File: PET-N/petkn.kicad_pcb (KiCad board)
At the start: 2 copper layers, 386.1 x 99.6 mm, 83 parts, among them J1 Conn_01x20, J2 Conn_02x03_Odd_Even, J3 LINK3, J4 Conn_01x20, J5 SPACE1, J6 SPACE2, J67 LINK67, SW1 KP "=", SW10 KP "0", SW11 R SHIFT, SW12 ">", SW14 "]", SW15 "@", SW16 L SHIFT, SW17 KP "+", SW18 KP "2", SW2 KP ".", SW20 "?", SW21 ",", SW22 "N", SW23 "V", SW24 "X", SW25 KP "3", SW26 KP "1", SW27 RETURN, SW28 ";", SW29 "M", SW3 NC ($10), SW30 "B", SW31 "C", SW32 "Z", SW320 S LOCK, SW33 KP "*", SW34 KP "5", SW36 ":", SW37 "K", SW38 "H", SW39 "F", SW4 STOP, SW40 "S", SW41 KP "6", SW42 KP "4", SW44 "L", SW45 "J", SW46 "G", SW47 "D", SW48 "A", SW49 KP "/", SW5 "<", SW50 KP "8", SW52 "P", SW53 "I", SW54 "Y", SW55 "R", SW56 "W", SW57 KP "9", SW58 KP "7", SW59 U ARROW, SW6 SPACE, SW60 "O", SW61 "U", SW62 "T", SW63 "E", SW64 "Q", SW65 INS/DEL, SW66 UP/DOWN, SW67 NC ($0A), SW68 ")", SW69 "\", SW7 "[", SW70 "'", SW71 "$", SW72 QUOTE, SW73 LEFT/RIGHT, SW74 CLR/HOME, SW75 B ARROW, SW76 "(", SW77 "&", SW78 "%", SW79 "#"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

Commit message: first work on adding LEDs and extended connector
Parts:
- removed J4: Conn_01x20, Connector_PinHeader_2.54mm:PinHeader_1x20_P2.54mm_Vertical
- J1: value Conn_01x20 -> Extended_PET_keyboard_connector; footprint Connector_PinHeader_2.54mm:PinHeader_1x20_P2.54mm_Vertical -> petkn:PET_Extended_Keyboard_Connector
- SW1, SW10, SW12, SW14, SW15, SW17, SW18, SW2, SW20, SW21, SW22, SW23, SW24, SW25, SW26, SW28, SW29, SW30, SW31, SW32, SW33, SW34, SW36, SW37, SW38, SW39, SW4, SW40, SW41, SW42, SW44, SW45, SW46, SW47, SW48, SW49, SW5, SW50, SW52, SW53, SW54, SW55, SW56, SW57, SW58, SW59, SW60, SW61, SW62, SW63, SW64, SW65, SW66, SW68, SW69, SW7, SW70, SW71, SW72, SW73, SW74, SW75, SW76, SW77, SW78, SW79, SW80, SW9: footprint Button_Switch_Keyboard:SW_Cherry_MX_1.00u_PCB -> petkn:SW_Cherry_MX_1.00u_PCB_with_LED
- SW11, SW16: footprint Button_Switch_Keyboard:SW_Cherry_MX_2.00u_PCB -> petkn:SW_Cherry_MX_2.00u_PCB_with_LED
- SW27, SW320, SW8: footprint Button_Switch_Keyboard:SW_Cherry_MX1A_1.50u_PCB -> petkn:SW_Cherry_MX_1.50u_PCB_with_LED
- SW3: footprint Button_Switch_Keyboard:SW_Cherry_MX1A_1.25u_PCB -> petkn:SW_Cherry_MX_1.25u_PCB_with_LED
- SW6: footprint Button_Switch_Keyboard:SW_Cherry_MX1A_6.25u_PCB -> petkn:SW_Cherry_MX_6.25u_PCB_with_LED
- SW67: footprint Button_Switch_Keyboard:SW_Cherry_MX_1.50u_PCB -> petkn:SW_Cherry_MX_1.50u_PCB_with_LED
- moved J1 1.93 mm to (234.1, 48.6)
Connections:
- J1 pad 1: (no net) -> GND
- J1 pad 2: (no net) -> unconnected-(J1-key-Pad2)
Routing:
- net C1: track 509.6 -> 371.9 mm
- net C2: track 509.5 -> 460.9 mm
- net R10: track 641.0 -> 598.0 mm, vias 1 -> 0
- net C4: track 304.8 -> 262.5 mm
- net C3: track 437.6 -> 405.7 mm
- net C6: track 504.1 -> 474.5 mm
- net R9: track 590.0 -> 563.2 mm
- net C5: track 252.0 -> 233.5 mm, vias 2 -> 1
- net C8: track 377.6 -> 371.5 mm
- net R2: track 601.0 -> 595.3 mm, vias 5 -> 6
- net R1: track 440.7 -> 437.4 mm, vias 4 -> 5
- net C7: track 345.6 -> 343.2 mm
- net R6: vias 4 -> 5
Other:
- board size 386.1 x 99.6 mm -> 386.1 x 102 mm
- board text added: "{dblquote}N-V2.1{dblquote} (C) A. Fachat, 2025-05-31"
- board text removed: "20 19 18 17 16 15 14 13 12 11 10 9 8 7 6 5 4 3 2 1"
- board text removed: "C1 C2 C3 C4 C5 C6 C7 C8 R1 R2 R3 R4 R5 R6 R7 R8 R9 R10 NC GND"

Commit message: add extension page, add 4-to-10 decoder
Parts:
- added C1: C, Capacitor_THT:C_Disc_D4.3mm_W1.9mm_P5.00mm, F.Cu at (303.7, 60.1)
- added U1: 74LS145, Package_DIP:DIP-16_W7.62mm, F.Cu at (302.5, 64.3)
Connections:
- SW1 pad 3: (no net) -> unconnected-(SW1B-K-Pad3)
- SW1 pad 4: (no net) -> unconnected-(SW1B-A-Pad4)
- SW10 pad 3: (no net) -> unconnected-(SW10B-K-Pad3)
- SW10 pad 4: (no net) -> unconnected-(SW10B-A-Pad4)
- SW11 pad 3: (no net) -> unconnected-(SW11B-K-Pad3)
- SW11 pad 4: (no net) -> unconnected-(SW11B-A-Pad4)
- SW12 pad 3: (no net) -> unconnected-(SW12B-K-Pad3)
- SW12 pad 4: (no net) -> unconnected-(SW12B-A-Pad4)
- SW14 pad 3: (no net) -> unconnected-(SW14B-K-Pad3)
- SW14 pad 4: (no net) -> unconnected-(SW14B-A-Pad4)
- SW15 pad 3: (no net) -> unconnected-(SW15B-K-Pad3)
- SW15 pad 4: (no net) -> unconnected-(SW15B-A-Pad4)
- SW16 pad 3: (no net) -> unconnected-(SW16B-K-Pad3)
- SW16 pad 4: (no net) -> unconnected-(SW16B-A-Pad4)
- SW17 pad 3: (no net) -> unconnected-(SW17B-K-Pad3)
- SW17 pad 4: (no net) -> unconnected-(SW17B-A-Pad4)
- SW18 pad 3: (no net) -> unconnected-(SW18B-K-Pad3)
- SW18 pad 4: (no net) -> unconnected-(SW18B-A-Pad4)
- SW2 pad 3: (no net) -> unconnected-(SW2B-K-Pad3)
- SW2 pad 4: (no net) -> unconnected-(SW2B-A-Pad4)
- SW20 pad 3: (no net) -> unconnected-(SW20B-K-Pad3)
- SW20 pad 4: (no net) -> unconnected-(SW20B-A-Pad4)
- SW21 pad 3: (no net) -> unconnected-(SW21B-K-Pad3)
- SW21 pad 4: (no net) -> unconnected-(SW21B-A-Pad4)
- SW22 pad 3: (no net) -> unconnected-(SW22B-K-Pad3)
- SW22 pad 4: (no net) -> unconnected-(SW22B-A-Pad4)
- SW23 pad 3: (no net) -> unconnected-(SW23B-K-Pad3)
- SW23 pad 4: (no net) -> unconnected-(SW23B-A-Pad4)
- SW24 pad 3: (no net) -> unconnected-(SW24B-K-Pad3)
- SW24 pad 4: (no net) -> unconnected-(SW24B-A-Pad4)
- SW25 pad 3: (no net) -> unconnected-(SW25B-K-Pad3)
- SW25 pad 4: (no net) -> unconnected-(SW25B-A-Pad4)
- SW26 pad 3: (no net) -> unconnected-(SW26B-K-Pad3)
- SW26 pad 4: (no net) -> unconnected-(SW26B-A-Pad4)
- SW27 pad 3: (no net) -> unconnected-(SW27B-K-Pad3)
- SW27 pad 4: (no net) -> unconnected-(SW27B-A-Pad4)
- SW28 pad 3: (no net) -> unconnected-(SW28B-K-Pad3)
- SW28 pad 4: (no net) -> unconnected-(SW28B-A-Pad4)
- SW29 pad 3: (no net) -> unconnected-(SW29B-K-Pad3)
- SW29 pad 4: (no net) -> unconnected-(SW29B-A-Pad4)
- SW3 pad 3: (no net) -> unconnected-(SW3B-K-Pad3)
- SW3 pad 4: (no net) -> unconnected-(SW3B-A-Pad4)
- SW30 pad 3: (no net) -> unconnected-(SW30B-K-Pad3)
- SW30 pad 4: (no net) -> unconnected-(SW30B-A-Pad4)
- SW31 pad 3: (no net) -> unconnected-(SW31B-K-Pad3)
- SW31 pad 4: (no net) -> unconnected-(SW31B-A-Pad4)
- SW32 pad 3: (no net) -> unconnected-(SW32B-K-Pad3)
- SW32 pad 4: (no net) -> unconnected-(SW32B-A-Pad4)
- SW320 pad 3: (no net) -> unconnected-(SW320B-K-Pad3)
- SW320 pad 4: (no net) -> unconnected-(SW320B-A-Pad4)
- SW33 pad 3: (no net) -> unconnected-(SW33B-K-Pad3)
- SW33 pad 4: (no net) -> unconnected-(SW33B-A-Pad4)
- SW34 pad 3: (no net) -> unconnected-(SW34B-K-Pad3)
- SW34 pad 4: (no net) -> unconnected-(SW34B-A-Pad4)
- SW36 pad 3: (no net) -> unconnected-(SW36B-K-Pad3)
- SW36 pad 4: (no net) -> unconnected-(SW36B-A-Pad4)
- SW37 pad 3: (no net) -> unconnected-(SW37B-K-Pad3)
- SW37 pad 4: (no net) -> unconnected-(SW37B-A-Pad4)
- SW38 pad 3: (no net) -> unconnected-(SW38B-K-Pad3)
- SW38 pad 4: (no net) -> unconnected-(SW38B-A-Pad4)
- SW39 pad 3: (no net) -> unconnected-(SW39B-K-Pad3)
- SW39 pad 4: (no net) -> unconnected-(SW39B-A-Pad4)
- SW4 pad 3: (no net) -> unconnected-(SW4B-K-Pad3)
- SW4 pad 4: (no net) -> unconnected-(SW4B-A-Pad4)
- SW40 pad 3: (no net) -> unconnected-(SW40B-K-Pad3)
- SW40 pad 4: (no net) -> unconnected-(SW40B-A-Pad4)
- SW41 pad 3: (no net) -> unconnected-(SW41B-K-Pad3)
- SW41 pad 4: (no net) -> unconnected-(SW41B-A-Pad4)
- SW42 pad 3: (no net) -> unconnected-(SW42B-K-Pad3)
- SW42 pad 4: (no net) -> unconnected-(SW42B-A-Pad4)
- SW44 pad 3: (no net) -> unconnected-(SW44B-K-Pad3)
- SW44 pad 4: (no net) -> unconnected-(SW44B-A-Pad4)
- SW45 pad 3: (no net) -> unconnected-(SW45B-K-Pad3)
- SW45 pad 4: (no net) -> unconnected-(SW45B-A-Pad4)
- SW46 pad 3: (no net) -> unconnected-(SW46B-K-Pad3)
- SW46 pad 4: (no net) -> unconnected-(SW46B-A-Pad4)
- SW47 pad 3: (no net) -> unconnected-(SW47B-K-Pad3)
- SW47 pad 4: (no net) -> unconnected-(SW47B-A-Pad4)
- SW48 pad 3: (no net) -> unconnected-(SW48B-K-Pad3)
- SW48 pad 4: (no net) -> unconnected-(SW48B-A-Pad4)
- SW49 pad 3: (no net) -> unconnected-(SW49B-K-Pad3)
- SW49 pad 4: (no net) -> unconnected-(SW49B-A-Pad4)
- SW5 pad 3: (no net) -> unconnected-(SW5B-K-Pad3)
- SW5 pad 4: (no net) -> unconnected-(SW5B-A-Pad4)
- SW50 pad 3: (no net) -> unconnected-(SW50B-K-Pad3)
- SW50 pad 4: (no net) -> unconnected-(SW50B-A-Pad4)
- SW52 pad 3: (no net) -> unconnected-(SW52B-K-Pad3)
- SW52 pad 4: (no net) -> unconnected-(SW52B-A-Pad4)
- SW53 pad 3: (no net) -> unconnected-(SW53B-K-Pad3)
- SW53 pad 4: (no net) -> unconnected-(SW53B-A-Pad4)
- SW54 pad 3: (no net) -> unconnected-(SW54B-K-Pad3)
- SW54 pad 4: (no net) -> unconnected-(SW54B-A-Pad4)
- SW55 pad 3: (no net) -> unconnected-(SW55B-K-Pad3)
- SW55 pad 4: (no net) -> unconnected-(SW55B-A-Pad4)
- SW56 pad 3: (no net) -> unconnected-(SW56B-K-Pad3)
- SW56 pad 4: (no net) -> unconnected-(SW56B-A-Pad4)
- SW57 pad 3: (no net) -> unconnected-(SW57B-K-Pad3)
- SW57 pad 4: (no net) -> unconnected-(SW57B-A-Pad4)
- SW58 pad 3: (no net) -> unconnected-(SW58B-K-Pad3)
- SW58 pad 4: (no net) -> unconnected-(SW58B-A-Pad4)
- SW59 pad 3: (no net) -> unconnected-(SW59B-K-Pad3)
- SW59 pad 4: (no net) -> unconnected-(SW59B-A-Pad4)
- SW6 pad 3: (no net) -> unconnected-(SW6B-K-Pad3)
- SW6 pad 4: (no net) -> unconnected-(SW6B-A-Pad4)
- SW60 pad 3: (no net) -> unconnected-(SW60B-K-Pad3)
- SW60 pad 4: (no net) -> unconnected-(SW60B-A-Pad4)
- SW61 pad 3: (no net) -> unconnected-(SW61B-K-Pad3)
- SW61 pad 4: (no net) -> unconnected-(SW61B-A-Pad4)
- SW62 pad 3: (no net) -> unconnected-(SW62B-K-Pad3)
- SW62 pad 4: (no net) -> unconnected-(SW62B-A-Pad4)
- SW63 pad 3: (no net) -> unconnected-(SW63B-K-Pad3)
- SW63 pad 4: (no net) -> unconnected-(SW63B-A-Pad4)
- SW64 pad 3: (no net) -> unconnected-(SW64B-K-Pad3)
- SW64 pad 4: (no net) -> unconnected-(SW64B-A-Pad4)
- SW65 pad 3: (no net) -> unconnected-(SW65B-K-Pad3)
- SW65 pad 4: (no net) -> unconnected-(SW65B-A-Pad4)
- SW66 pad 3: (no net) -> unconnected-(SW66B-K-Pad3)
- SW66 pad 4: (no net) -> unconnected-(SW66B-A-Pad4)
- SW67 pad 3: (no net) -> unconnected-(SW67B-K-Pad3)
- SW67 pad 4: (no net) -> unconnected-(SW67B-A-Pad4)
- SW68 pad 3: (no net) -> unconnected-(SW68B-K-Pad3)
- SW68 pad 4: (no net) -> unconnected-(SW68B-A-Pad4)
- SW69 pad 3: (no net) -> unconnected-(SW69B-K-Pad3)
- SW69 pad 4: (no net) -> unconnected-(SW69B-A-Pad4)
- SW7 pad 3: (no net) -> unconnected-(SW7B-K-Pad3)
- SW7 pad 4: (no net) -> unconnected-(SW7B-A-Pad4)
- SW70 pad 3: (no net) -> unconnected-(SW70B-K-Pad3)
- SW70 pad 4: (no net) -> unconnected-(SW70B-A-Pad4)
- SW71 pad 3: (no net) -> unconnected-(SW71B-K-Pad3)
- SW71 pad 4: (no net) -> unconnected-(SW71B-A-Pad4)
- SW72 pad 3: (no net) -> unconnected-(SW72B-K-Pad3)
- SW72 pad 4: (no net) -> unconnected-(SW72B-A-Pad4)
- SW73 pad 3: (no net) -> unconnected-(SW73B-K-Pad3)
- SW73 pad 4: (no net) -> unconnected-(SW73B-A-Pad4)
- SW74 pad 3: (no net) -> unconnected-(SW74B-K-Pad3)
- SW74 pad 4: (no net) -> unconnected-(SW74B-A-Pad4)
- SW75 pad 3: (no net) -> unconnected-(SW75B-K-Pad3)
- SW75 pad 4: (no net) -> unconnected-(SW75B-A-Pad4)
- SW76 pad 3: (no net) -> unconnected-(SW76B-K-Pad3)
- SW76 pad 4: (no net) -> unconnected-(SW76B-A-Pad4)
- SW77 pad 3: (no net) -> unconnected-(SW77B-K-Pad3)
- SW77 pad 4: (no net) -> unconnected-(SW77B-A-Pad4)
- SW78 pad 3: (no net) -> unconnected-(SW78B-K-Pad3)
- SW78 pad 4: (no net) -> unconnected-(SW78B-A-Pad4)
- SW79 pad 3: (no net) -> unconnected-(SW79B-K-Pad3)
- SW79 pad 4: (no net) -> unconnected-(SW79B-A-Pad4)
- SW8 pad 3: (no net) -> unconnected-(SW8B-K-Pad3)
- SW8 pad 4: (no net) -> unconnected-(SW8B-A-Pad4)
- SW80 pad 3: (no net) -> unconnected-(SW80B-K-Pad3)
- SW80 pad 4: (no net) -> unconnected-(SW80B-A-Pad4)
- SW9 pad 3: (no net) -> unconnected-(SW9B-K-Pad3)
- SW9 pad 4: (no net) -> unconnected-(SW9B-A-Pad4)
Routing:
- net R10: track 598.0 -> 0.00 mm
- net R2: track 595.3 -> 0.00 mm, vias 6 -> 0
- net R9: track 563.2 -> 0.00 mm, vias 5 -> 0
- net R4: track 532.2 -> 0.00 mm, vias 3 -> 0
- net C6: track 474.5 -> 0.00 mm, vias 6 -> 0
- net C2: track 460.9 -> 0.00 mm, vias 4 -> 0
- net R1: track 437.4 -> 0.00 mm, vias 5 -> 0
- net R8: track 430.2 -> 0.00 mm, vias 3 -> 0
- net R6: track 414.2 -> 0.00 mm, vias 5 -> 0
- net R7: track 410.3 -> 0.00 mm, vias 3 -> 0
- net C3: track 405.7 -> 0.00 mm, vias 2 -> 0
- net R3: track 384.7 -> 0.00 mm, vias 3 -> 0
- net R5: track 374.0 -> 0.00 mm, vias 1 -> 0
- net C1: track 371.9 -> 0.00 mm, vias 3 -> 0
- net C8: track 371.5 -> 0.00 mm, vias 1 -> 0
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
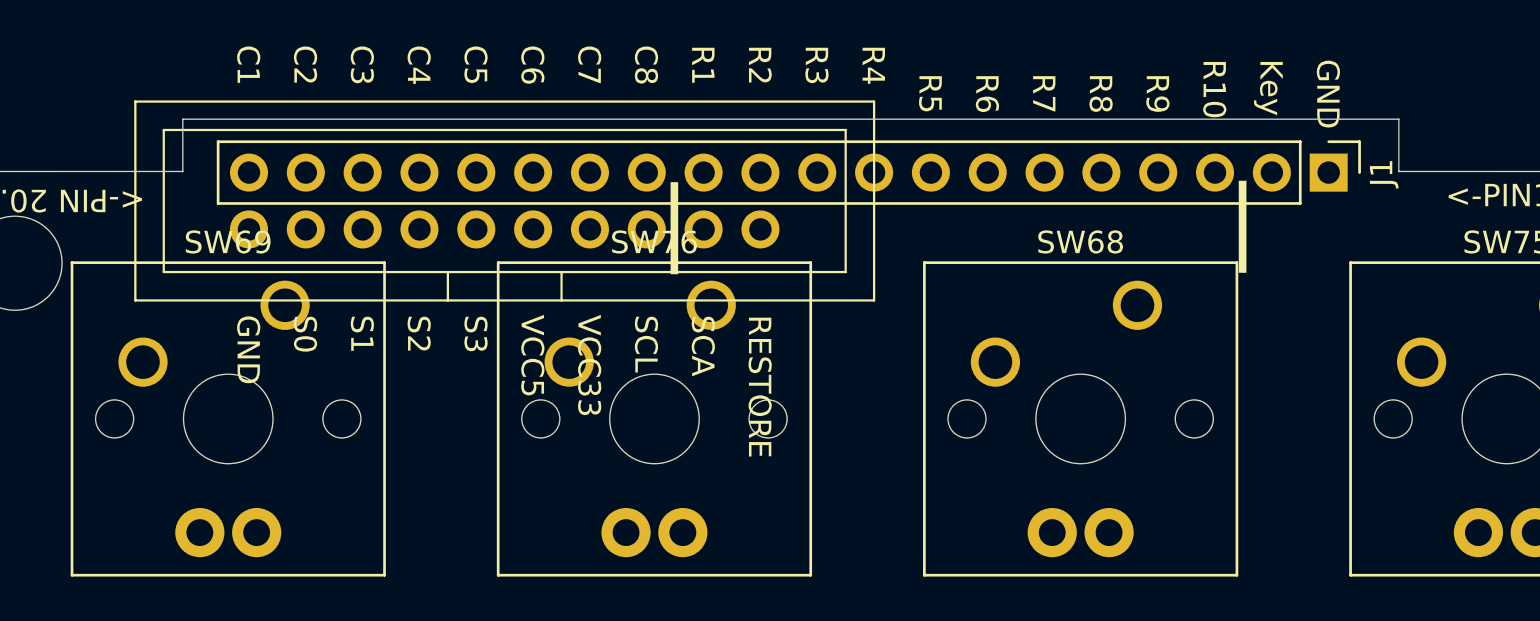
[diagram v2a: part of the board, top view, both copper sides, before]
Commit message: test board for LED drivers
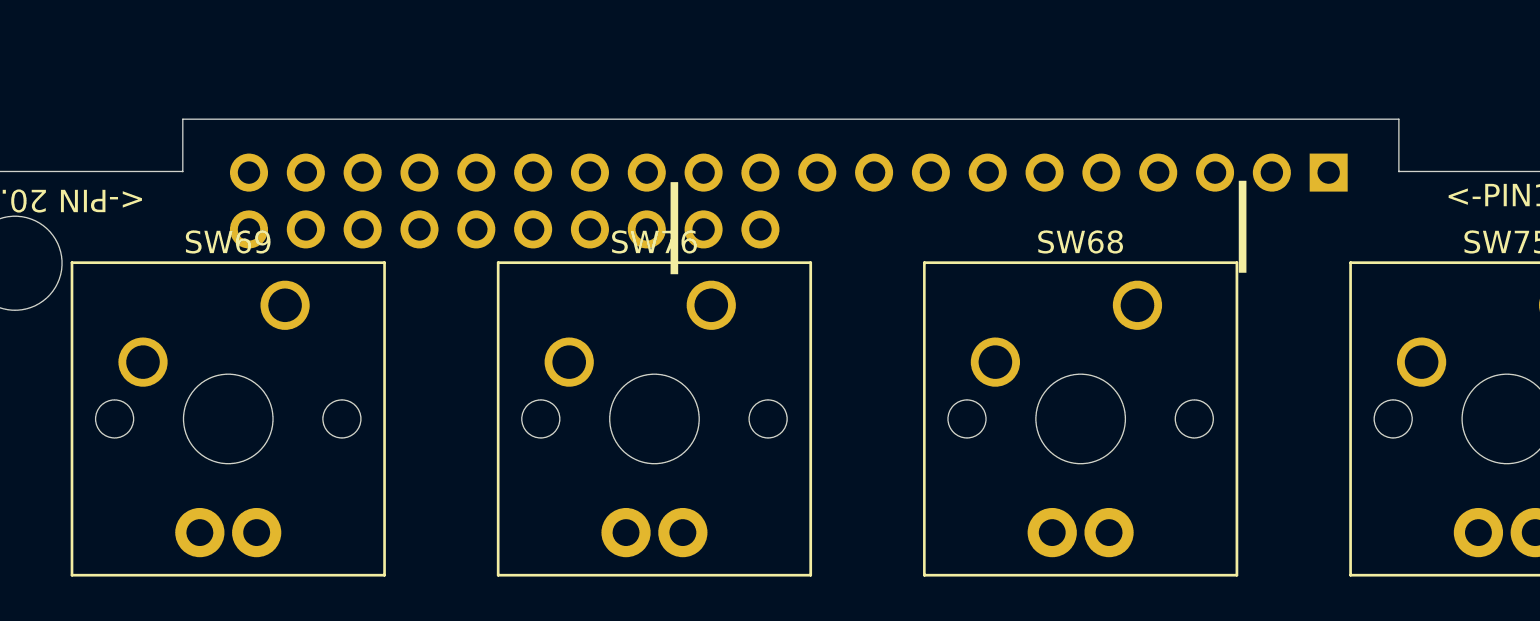
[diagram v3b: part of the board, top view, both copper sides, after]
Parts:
- J1: moved to B.Cu
- turned J1 to 90 degrees

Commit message: work on R3 of keyboard pcb
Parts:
- added C2: C, Capacitor_SMD:C_0603_1608Metric_Pad1.08x0.95mm_HandSolder, F.Cu at (105.3, 25.1)
- added C3: C, Capacitor_SMD:C_0603_1608Metric_Pad1.08x0.95mm_HandSolder, F.Cu at (105.3, 18.1)
- added C4: C, Capacitor_SMD:C_0603_1608Metric_Pad1.08x0.95mm_HandSolder, F.Cu at (105.3, 20.6)
- added C5: 100u, Capacitor_SMD:C_1206_3216Metric_Pad1.33x1.80mm_HandSolder, F.Cu at (97.2, 20.5)
- added C6: 100u, Capacitor_SMD:C_1206_3216Metric_Pad1.33x1.80mm_HandSolder, F.Cu at (97.2, 23.9)
- added C7: 100u, Capacitor_SMD:C_1206_3216Metric_Pad1.33x1.80mm_HandSolder, F.Cu at (97.2, 27.2)
- added J4: LINK3, Connector_PinHeader_2.54mm:PinHeader_2x02_P2.54mm_Vertical, F.Cu at (293.1, 59.5)
- added Q1: BC859, Package_TO_SOT_SMD:SOT-23, F.Cu at (345.7, 153.0)
- added Q10: BC808, Package_TO_SOT_SMD:SOT-23, F.Cu at (277.5, 153.2)
- added Q11: BC848, Package_TO_SOT_SMD:SOT-23, F.Cu at (271.7, 158.1)
- added Q12: BC808, Package_TO_SOT_SMD:SOT-23, F.Cu at (277.5, 158.1)
- added Q13: BC848, Package_TO_SOT_SMD:SOT-23, F.Cu at (303.5, 153.5)
- added Q14: BC808, Package_TO_SOT_SMD:SOT-23, F.Cu at (309.0, 153.5)
- added Q15: BC848, Package_TO_SOT_SMD:SOT-23, F.Cu at (303.4, 158.5)
- added Q16: BC808, Package_TO_SOT_SMD:SOT-23, F.Cu at (309.2, 158.5)
- added Q17: BC848, Package_TO_SOT_SMD:SOT-23, F.Cu at (317.6, 153.5)
- added Q18: BC808, Package_TO_SOT_SMD:SOT-23, F.Cu at (323.5, 153.4)
- added Q19: BC848, Package_TO_SOT_SMD:SOT-23, F.Cu at (317.3, 158.5)
- added Q2: BC859, Package_TO_SOT_SMD:SOT-23, F.Cu at (345.7, 163.0)
- added Q20: BC808, Package_TO_SOT_SMD:SOT-23, F.Cu at (323.0, 158.5)
- added Q21: BC848, Package_TO_SOT_SMD:SOT-23, F.Cu at (288.7, 153.4)
- added Q22: BC808, Package_TO_SOT_SMD:SOT-23, F.Cu at (294.4, 153.3)
- added Q23: BC848, Package_TO_SOT_SMD:SOT-23, F.Cu at (288.8, 158.4)
- added Q24: BC808, Package_TO_SOT_SMD:SOT-23, F.Cu at (294.4, 158.4)
- added Q25: BC859, Package_TO_SOT_SMD:SOT-23, F.Cu at (247.3, 153.7)
- added Q26: BC859, Package_TO_SOT_SMD:SOT-23, F.Cu at (247.3, 158.8)
- added Q27: BC859, Package_TO_SOT_SMD:SOT-23, F.Cu at (247.4, 164.5)
- added Q28: BC859, Package_TO_SOT_SMD:SOT-23, F.Cu at (247.5, 171.0)
- added Q29: BC848, Package_TO_SOT_SMD:SOT-23, F.Cu at (287.8, 144.5)
- added Q3: BC859, Package_TO_SOT_SMD:SOT-23, F.Cu at (345.7, 168.2)
- added Q30: BC848, Package_TO_SOT_SMD:SOT-23, F.Cu at (287.8, 140.1)
- added Q31: BC848, Package_TO_SOT_SMD:SOT-23, F.Cu at (287.9, 130.8)
- added Q32: BC848, Package_TO_SOT_SMD:SOT-23, F.Cu at (287.9, 135.0)
- added Q4: BC859, Package_TO_SOT_SMD:SOT-23, F.Cu at (354.5, 152.9)
- added Q5: BC859, Package_TO_SOT_SMD:SOT-23, F.Cu at (345.7, 158.1)
- added Q6: BC859, Package_TO_SOT_SMD:SOT-23, F.Cu at (354.5, 158.1)
- added Q7: BC859, Package_TO_SOT_SMD:SOT-23, F.Cu at (354.6, 163.0)
- added Q8: BC859, Package_TO_SOT_SMD:SOT-23, F.Cu at (354.6, 168.1)
- added Q9: BC848, Package_TO_SOT_SMD:SOT-23, F.Cu at (271.7, 153.1)
- added R1: 100k, Resistor_SMD:R_0805_2012Metric, F.Cu at (350.8, 169.1)
- added R10: 100k, Resistor_SMD:R_0805_2012Metric, F.Cu at (313.9, 152.4)
- added R100: 390, Resistor_SMD:R_0805_2012Metric, F.Cu at (315.7, 102.4)
- added R101: 390, Resistor_SMD:R_0805_2012Metric, F.Cu at (334.9, 102.6)
- added R102: 390, Resistor_SMD:R_0805_2012Metric, F.Cu at (353.8, 102.7)
- added R103: 390, Resistor_SMD:R_0805_2012Metric, F.Cu at (372.7, 102.6)
- added R104: 390, Resistor_SMD:R_0805_2012Metric, F.Cu at (28.8, 121.4)
- added R105: 390, Resistor_SMD:R_0805_2012Metric, F.Cu at (66.9, 121.5)
- added R106: 390, Resistor_SMD:R_0805_2012Metric, F.Cu at (86.0, 121.6)
- added R107: 390, Resistor_SMD:R_0805_2012Metric, F.Cu at (105.1, 121.6)
- added R108: 390, Resistor_SMD:R_0805_2012Metric, F.Cu at (124.1, 121.6)
- added R109: 390, Resistor_SMD:R_0805_2012Metric, F.Cu at (143.1, 121.6)
- added R11: 100k, Resistor_SMD:R_0805_2012Metric, F.Cu at (320.5, 153.4)
- added R110: 390, Resistor_SMD:R_0805_2012Metric, F.Cu at (162.1, 121.6)
- added R111: 390, Resistor_SMD:R_0805_2012Metric, F.Cu at (181.3, 121.7)
- added R112: 390, Resistor_SMD:R_0805_2012Metric, F.Cu at (200.3, 121.6)
- added R113: 390, Resistor_SMD:R_0805_2012Metric, F.Cu at (219.2, 121.6)
- added R114: 390, Resistor_SMD:R_0805_2012Metric, F.Cu at (238.3, 121.5)
- added R115: 390, Resistor_SMD:R_0805_2012Metric, F.Cu at (257.5, 121.5)
- added R116: 390, Resistor_SMD:R_0805_2012Metric, F.Cu at (153.9, 140.8)
- added R117: 390, Resistor_SMD:R_0805_2012Metric, F.Cu at (225.3, 140.6)
- added R118: 390, Resistor_SMD:R_0805_2012Metric, F.Cu at (315.9, 121.5)
- added R119: 390, Resistor_SMD:R_0805_2012Metric, F.Cu at (334.8, 121.7)
- added R12: 100k, Resistor_SMD:R_0805_2012Metric, F.Cu at (313.6, 159.5)
- added R120: 390, Resistor_SMD:R_0805_2012Metric, F.Cu at (353.9, 121.7)
- added R121: 390, Resistor_SMD:R_0805_2012Metric, F.Cu at (372.8, 121.7)
- added R122: 390, Resistor_SMD:R_0805_2012Metric, F.Cu at (315.8, 140.8)
- added R123: 390, Resistor_SMD:R_0805_2012Metric, F.Cu at (334.8, 140.7)
- added R124: 390, Resistor_SMD:R_0805_2012Metric, F.Cu at (353.8, 140.5)
- added R125: 390, Resistor_SMD:R_0805_2012Metric, F.Cu at (372.8, 140.7)
- added R126: 100k, Resistor_SMD:R_0805_2012Metric, F.Cu at (291.9, 145.4)
- added R127: 10k, Resistor_SMD:R_0805_2012Metric, F.Cu at (291.9, 143.4)
- added R128: 10k, Resistor_SMD:R_0805_2012Metric, F.Cu at (291.9, 139.1)
- added R129: 100k, Resistor_SMD:R_0805_2012Metric, F.Cu at (291.9, 141.1)
- added R13: 100k, Resistor_SMD:R_0805_2012Metric, F.Cu at (313.6, 157.4)
- added R130: 10k, Resistor_SMD:R_0805_2012Metric, F.Cu at (291.9, 129.8)
- added R131: 10k, Resistor_SMD:R_0805_2012Metric, F.Cu at (291.8, 134.0)
- added R132: 100k, Resistor_SMD:R_0805_2012Metric, F.Cu at (291.8, 131.8)
- added R133: 100k, Resistor_SMD:R_0805_2012Metric, F.Cu at (291.8, 136.0)
- added R14: 100k, Resistor_SMD:R_0805_2012Metric, F.Cu at (320.1, 158.5)
- added R15: 100k, Resistor_SMD:R_0805_2012Metric, F.Cu at (284.6, 154.7)
- added R16: 100k, Resistor_SMD:R_0805_2012Metric, F.Cu at (284.6, 152.3)
- added R17: 100k, Resistor_SMD:R_0805_2012Metric, F.Cu at (291.5, 153.3)
- added R18: 100k, Resistor_SMD:R_0805_2012Metric, F.Cu at (284.6, 159.5)
- added R19: 100k, Resistor_SMD:R_0805_2012Metric, F.Cu at (284.6, 157.4)
- added R2: 100k, Resistor_SMD:R_0805_2012Metric, F.Cu at (350.8, 163.9)
- added R20: 100k, Resistor_SMD:R_0805_2012Metric, F.Cu at (291.6, 158.4)
- added R21: 100k, Resistor_SMD:R_0805_2012Metric, F.Cu at (341.6, 157.0)
- added R22: 100k, Resistor_SMD:R_0805_2012Metric, F.Cu at (341.5, 152.0)
- added R23: 100k, Resistor_SMD:R_0805_2012Metric, F.Cu at (341.7, 162.1)
- added R24: 100k, Resistor_SMD:R_0805_2012Metric, F.Cu at (341.7, 167.2)
- added R25: 100k, Resistor_SMD:R_0805_2012Metric, F.Cu at (220.3, 153.0)
- added R26: 100k, Resistor_SMD:R_0805_2012Metric, F.Cu at (341.5, 153.8)
- added R27: 100k, Resistor_SMD:R_0805_2012Metric, F.Cu at (341.7, 164.0)
- added R28: 100k, Resistor_SMD:R_0805_2012Metric, F.Cu at (341.7, 169.1)
- added R29: 100k, Resistor_SMD:R_0805_2012Metric, F.Cu at (243.4, 172.1)
- added R3: 100k, Resistor_SMD:R_0805_2012Metric, F.Cu at (350.8, 159.1)
- added R30: 100k, Resistor_SMD:R_0805_2012Metric, F.Cu at (341.6, 159.1)
- added R31: 100k, Resistor_SMD:R_0805_2012Metric, F.Cu at (274.6, 153.2)
- added R32: 100k, Resistor_SMD:R_0805_2012Metric, F.Cu at (267.5, 152.1)
- added R33: 100k, Resistor_SMD:R_0805_2012Metric, F.Cu at (267.5, 154.2)
- added R34: 100k, Resistor_SMD:R_0805_2012Metric, F.Cu at (267.7, 159.1)
- added R35: 100k, Resistor_SMD:R_0805_2012Metric, F.Cu at (267.5, 156.9)
- added R36: 100k, Resistor_SMD:R_0805_2012Metric, F.Cu at (274.6, 158.2)
- added R37: 100k, Resistor_SMD:R_0805_2012Metric, F.Cu at (299.6, 154.6)
- added R38: 100k, Resistor_SMD:R_0805_2012Metric, F.Cu at (299.6, 152.5)
- added R39: 100k, Resistor_SMD:R_0805_2012Metric, F.Cu at (306.3, 153.6)
- added R4: 100k, Resistor_SMD:R_0805_2012Metric, F.Cu at (350.6, 153.9)
- added R40: 100k, Resistor_SMD:R_0805_2012Metric, F.Cu at (299.7, 159.6)
- added R41: 100k, Resistor_SMD:R_0805_2012Metric, F.Cu at (299.6, 157.4)
- added R42: 100k, Resistor_SMD:R_0805_2012Metric, F.Cu at (306.3, 158.5)
- added R43: 100k, Resistor_SMD:R_0805_2012Metric, F.Cu at (243.2, 165.7)
- added R44: 100k, Resistor_SMD:R_0805_2012Metric, F.Cu at (243.1, 159.8)
- added R45: 100k, Resistor_SMD:R_0805_2012Metric, F.Cu at (243.0, 154.7)
- added R46: 100k, Resistor_SMD:R_0805_2012Metric, F.Cu at (243.0, 152.7)
- added R47: 100k, Resistor_SMD:R_0805_2012Metric, F.Cu at (243.1, 157.8)
- added R48: 100k, Resistor_SMD:R_0805_2012Metric, F.Cu at (243.1, 163.6)
- added R49: 100k, Resistor_SMD:R_0805_2012Metric, F.Cu at (243.3, 170.0)
- added R5: 100k, Resistor_SMD:R_0805_2012Metric, F.Cu at (350.6, 152.0)
- added R50: 390, Resistor_SMD:R_0805_2012Metric, F.Cu at (24.0, 64.4)
- added R51: 390, Resistor_SMD:R_0805_2012Metric, F.Cu at (43.0, 64.5)
- added R52: 390, Resistor_SMD:R_0805_2012Metric, F.Cu at (62.2, 64.4)
- added R53: 390, Resistor_SMD:R_0805_2012Metric, F.Cu at (81.1, 64.3)
- added R54: 390, Resistor_SMD:R_0805_2012Metric, F.Cu at (100.2, 64.4)
- added R55: 390, Resistor_SMD:R_0805_2012Metric, F.Cu at (119.2, 64.4)
- added R56: 390, Resistor_SMD:R_0805_2012Metric, F.Cu at (138.3, 64.3)
- added R57: 390, Resistor_SMD:R_0805_2012Metric, F.Cu at (157.4, 64.3)
- added R58: 390, Resistor_SMD:R_0805_2012Metric, F.Cu at (176.5, 64.3)
- added R59: 390, Resistor_SMD:R_0805_2012Metric, F.Cu at (195.5, 64.3)
- added R6: 100k, Resistor_SMD:R_0805_2012Metric, F.Cu at (350.8, 157.1)
- added R60: 390, Resistor_SMD:R_0805_2012Metric, F.Cu at (214.4, 64.4)
- added R61: 390, Resistor_SMD:R_0805_2012Metric, F.Cu at (233.5, 64.3)
- added R62: 390, Resistor_SMD:R_0805_2012Metric, F.Cu at (252.6, 64.3)
- added R63: 390, Resistor_SMD:R_0805_2012Metric, F.Cu at (271.6, 64.3)
- added R64: 390, Resistor_SMD:R_0805_2012Metric, F.Cu at (315.7, 64.4)
- added R65: 390, Resistor_SMD:R_0805_2012Metric, F.Cu at (334.8, 64.3)
- added R66: 390, Resistor_SMD:R_0805_2012Metric, F.Cu at (353.7, 64.3)
- added R67: 390, Resistor_SMD:R_0805_2012Metric, F.Cu at (372.8, 64.3)
- added R68: 390, Resistor_SMD:R_0805_2012Metric, F.Cu at (23.9, 83.6)
- added R69: 390, Resistor_SMD:R_0805_2012Metric, F.Cu at (52.6, 83.6)
- added R7: 100k, Resistor_SMD:R_0805_2012Metric, F.Cu at (350.8, 162.1)
- added R70: 390, Resistor_SMD:R_0805_2012Metric, F.Cu at (71.5, 83.6)
- added R71: 390, Resistor_SMD:R_0805_2012Metric, F.Cu at (90.6, 83.5)
- added R72: 390, Resistor_SMD:R_0805_2012Metric, F.Cu at (109.6, 83.5)
- added R73: 390, Resistor_SMD:R_0805_2012Metric, F.Cu at (128.8, 83.5)
- added R74: 390, Resistor_SMD:R_0805_2012Metric, F.Cu at (147.8, 83.6)
- added R75: 390, Resistor_SMD:R_0805_2012Metric, F.Cu at (166.8, 83.5)
- added R76: 390, Resistor_SMD:R_0805_2012Metric, F.Cu at (186.0, 83.5)
- added R77: 390, Resistor_SMD:R_0805_2012Metric, F.Cu at (205.0, 83.5)
- added R78: 390, Resistor_SMD:R_0805_2012Metric, F.Cu at (223.9, 83.6)
- added R79: 390, Resistor_SMD:R_0805_2012Metric, F.Cu at (243.1, 83.4)
- added R8: 100k, Resistor_SMD:R_0805_2012Metric, F.Cu at (350.8, 167.1)
- added R80: 390, Resistor_SMD:R_0805_2012Metric, F.Cu at (262.1, 83.5)
- added R81: 390, Resistor_SMD:R_0805_2012Metric, F.Cu at (281.1, 83.6)
- added R82: 390, Resistor_SMD:R_0805_2012Metric, F.Cu at (315.6, 83.5)
- added R83: 390, Resistor_SMD:R_0805_2012Metric, F.Cu at (334.9, 83.6)
- added R84: 390, Resistor_SMD:R_0805_2012Metric, F.Cu at (353.7, 83.4)
- added R85: 390, Resistor_SMD:R_0805_2012Metric, F.Cu at (372.8, 83.5)
- added R86: 390, Resistor_SMD:R_0805_2012Metric, F.Cu at (29.0, 102.4)
- added R87: 390, Resistor_SMD:R_0805_2012Metric, F.Cu at (57.4, 102.5)
- added R88: 390, Resistor_SMD:R_0805_2012Metric, F.Cu at (76.6, 102.6)
- added R89: 390, Resistor_SMD:R_0805_2012Metric, F.Cu at (95.6, 102.5)
- added R9: 100k, Resistor_SMD:R_0805_2012Metric, F.Cu at (313.9, 154.5)
- added R90: 390, Resistor_SMD:R_0805_2012Metric, F.Cu at (114.5, 102.4)
- added R91: 390, Resistor_SMD:R_0805_2012Metric, F.Cu at (133.6, 102.5)
- added R92: 390, Resistor_SMD:R_0805_2012Metric, F.Cu at (152.6, 102.5)
- added R93: 390, Resistor_SMD:R_0805_2012Metric, F.Cu at (171.9, 102.4)
- added R94: 390, Resistor_SMD:R_0805_2012Metric, F.Cu at (191.0, 102.4)
- added R95: 390, Resistor_SMD:R_0805_2012Metric, F.Cu at (209.8, 102.6)
- added R96: 390, Resistor_SMD:R_0805_2012Metric, F.Cu at (228.9, 102.5)
- added R97: 390, Resistor_SMD:R_0805_2012Metric, F.Cu at (247.9, 102.4)
- added R98: 390, Resistor_SMD:R_0805_2012Metric, F.Cu at (267.3, 102.6)
- added R99: 390, Resistor_SMD:R_0805_2012Metric, F.Cu at (80.6, 140.6)
- added U2: PCA9557PW, Package_SO:TSSOP-16_4.4x5mm_P0.65mm, F.Cu at (307.0, 91.2)
- added U3: PCA9531PW, Package_SO:TSSOP-16_4.4x5mm_P0.65mm, F.Cu at (307.0, 110.6)
- added U4: PCA9531PW, Package_SO:TSSOP-16_4.4x5mm_P0.65mm, F.Cu at (306.9, 101.0)
- added U5: ~, petkn:THB Miniature Thumbstick THB001P, F.Cu at (304.6, 130.2)
- C1: footprint Capacitor_THT:C_Disc_D4.3mm_W1.9mm_P5.00mm -> Capacitor_SMD:C_0603_1608Metric_Pad1.08x0.95mm_HandSolder
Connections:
- net VCC5 renamed VCC
- SW1 pad 3: unconnected-(SW1B-K-Pad3) -> Net-(SW1B-K)
- SW1 pad 4: unconnected-(SW1B-A-Pad4) -> HI3
- SW10 pad 3: unconnected-(SW10B-K-Pad3) -> Net-(SW10B-K)
- SW11 pad 3: unconnected-(SW11B-K-Pad3) -> Net-(SW11B-K)
- SW11 pad 4: unconnected-(SW11B-A-Pad4) -> HI7
- SW12 pad 3: unconnected-(SW12B-K-Pad3) -> Net-(SW12B-K)
- SW12 pad 4: unconnected-(SW12B-A-Pad4) -> HI4
- SW14 pad 3: unconnected-(SW14B-K-Pad3) -> Net-(SW14B-K)
- SW14 pad 4: unconnected-(SW14B-A-Pad4) -> HI4
- SW15 pad 3: unconnected-(SW15B-K-Pad3) -> Net-(SW15B-K)
- SW15 pad 4: unconnected-(SW15B-A-Pad4) -> HI4
- SW16 pad 3: unconnected-(SW16B-K-Pad3) -> Net-(SW16B-K)
- SW16 pad 4: unconnected-(SW16B-A-Pad4) -> HI4
- SW17 pad 3: unconnected-(SW17B-K-Pad3) -> Net-(SW17B-K)
- SW17 pad 4: unconnected-(SW17B-A-Pad4) -> HI3
- SW18 pad 3: unconnected-(SW18B-K-Pad3) -> Net-(SW18B-K)
- SW18 pad 4: unconnected-(SW18B-A-Pad4) -> HI1
- SW2 pad 3: unconnected-(SW2B-K-Pad3) -> Net-(R123-Pad1)
- SW2 pad 4: unconnected-(SW2B-A-Pad4) -> HI1
- SW20 pad 3: unconnected-(SW20B-K-Pad3) -> Net-(SW20B-K)
- SW20 pad 4: unconnected-(SW20B-A-Pad4) -> HI6
- SW21 pad 3: unconnected-(SW21B-K-Pad3) -> Net-(SW21B-K)
- SW21 pad 4: unconnected-(SW21B-A-Pad4) -> HI7
- SW22 pad 3: unconnected-(SW22B-K-Pad3) -> Net-(SW22B-K)
- SW22 pad 4: unconnected-(SW22B-A-Pad4) -> HI5
- SW23 pad 3: unconnected-(SW23B-K-Pad3) -> Net-(SW23B-K)
- SW23 pad 4: unconnected-(SW23B-A-Pad4) -> HI3
- SW24 pad 3: unconnected-(SW24B-K-Pad3) -> Net-(SW24B-K)
- SW24 pad 4: unconnected-(SW24B-A-Pad4) -> HI1
- SW25 pad 3: unconnected-(SW25B-K-Pad3) -> Net-(SW25B-K)
- SW25 pad 4: unconnected-(SW25B-A-Pad4) -> HI2
- SW26 pad 3: unconnected-(SW26B-K-Pad3) -> Net-(SW26B-K)
- SW26 pad 4: unconnected-(SW26B-A-Pad4) -> HI0
- SW27 pad 3: unconnected-(SW27B-K-Pad3) -> Net-(SW27B-K)
- SW28 pad 3: unconnected-(SW28B-K-Pad3) -> Net-(SW28B-K)
- SW28 pad 4: unconnected-(SW28B-A-Pad4) -> HI5
- SW29 pad 3: unconnected-(SW29B-K-Pad3) -> Net-(SW29B-K)
- SW29 pad 4: unconnected-(SW29B-A-Pad4) -> HI6
- SW3 pad 3: unconnected-(SW3B-K-Pad3) -> Net-(R117-Pad1)
- SW3 pad 4: unconnected-(SW3B-A-Pad4) -> HI6
- SW30 pad 3: unconnected-(SW30B-K-Pad3) -> Net-(SW30B-K)
- SW30 pad 4: unconnected-(SW30B-A-Pad4) -> HI4
- SW31 pad 3: unconnected-(SW31B-K-Pad3) -> Net-(SW31B-K)
- SW31 pad 4: unconnected-(SW31B-A-Pad4) -> HI2
- SW32 pad 3: unconnected-(SW32B-K-Pad3) -> Net-(SW32B-K)
- SW32 pad 4: unconnected-(SW32B-A-Pad4) -> HI0
- SW320 pad 3: unconnected-(SW320B-K-Pad3) -> Net-(R86-Pad1)
- SW320 pad 4: unconnected-(SW320B-A-Pad4) -> HI4
- SW33 pad 3: unconnected-(SW33B-K-Pad3) -> Net-(SW33B-K)
- SW33 pad 4: unconnected-(SW33B-A-Pad4) -> HI3
- SW34 pad 3: unconnected-(SW34B-K-Pad3) -> Net-(SW34B-K)
- SW34 pad 4: unconnected-(SW34B-A-Pad4) -> HI1
- SW36 pad 3: unconnected-(SW36B-K-Pad3) -> Net-(SW36B-K)
- SW36 pad 4: unconnected-(SW36B-A-Pad4) -> HI1
- SW37 pad 3: unconnected-(SW37B-K-Pad3) -> Net-(SW37B-K)
- SW37 pad 4: unconnected-(SW37B-A-Pad4) -> HI7
- SW38 pad 3: unconnected-(SW38B-K-Pad3) -> Net-(SW38B-K)
- SW38 pad 4: unconnected-(SW38B-A-Pad4) -> HI5
- SW39 pad 3: unconnected-(SW39B-K-Pad3) -> Net-(SW39B-K)
- SW39 pad 4: unconnected-(SW39B-A-Pad4) -> HI3
- SW4 pad 3: unconnected-(SW4B-K-Pad3) -> Net-(SW4B-K)
- SW40 pad 3: unconnected-(SW40B-K-Pad3) -> Net-(SW40B-K)
- SW40 pad 4: unconnected-(SW40B-A-Pad4) -> HI1
- SW41 pad 3: unconnected-(SW41B-K-Pad3) -> Net-(SW41B-K)
- SW41 pad 4: unconnected-(SW41B-A-Pad4) -> HI2
- SW42 pad 3: unconnected-(SW42B-K-Pad3) -> Net-(SW42B-K)
- SW42 pad 4: unconnected-(SW42B-A-Pad4) -> HI0
- SW44 pad 3: unconnected-(SW44B-K-Pad3) -> Net-(SW44B-K)
- SW44 pad 4: unconnected-(SW44B-A-Pad4) -> HI0
- SW45 pad 3: unconnected-(SW45B-K-Pad3) -> Net-(SW45B-K)
- SW45 pad 4: unconnected-(SW45B-A-Pad4) -> HI6
- SW46 pad 3: unconnected-(SW46B-K-Pad3) -> Net-(SW46B-K)
- SW46 pad 4: unconnected-(SW46B-A-Pad4) -> HI4
- SW47 pad 3: unconnected-(SW47B-K-Pad3) -> Net-(SW47B-K)
- SW47 pad 4: unconnected-(SW47B-A-Pad4) -> HI2
- SW48 pad 3: unconnected-(SW48B-K-Pad3) -> Net-(SW48B-K)
- SW48 pad 4: unconnected-(SW48B-A-Pad4) -> HI0
- SW49 pad 3: unconnected-(SW49B-K-Pad3) -> Net-(SW49B-K)
- SW49 pad 4: unconnected-(SW49B-A-Pad4) -> HI3
- SW5 pad 3: unconnected-(SW5B-K-Pad3) -> Net-(SW5B-K)
- SW5 pad 4: unconnected-(SW5B-A-Pad4) -> HI3
- SW50 pad 3: unconnected-(SW50B-K-Pad3) -> Net-(SW50B-K)
- SW50 pad 4: unconnected-(SW50B-A-Pad4) -> HI1
- SW52 pad 3: unconnected-(SW52B-K-Pad3) -> Net-(SW52B-K)
- SW52 pad 4: unconnected-(SW52B-A-Pad4) -> HI1
- SW53 pad 3: unconnected-(SW53B-K-Pad3) -> Net-(SW53B-K)
- SW53 pad 4: unconnected-(SW53B-A-Pad4) -> HI7
- SW54 pad 3: unconnected-(SW54B-K-Pad3) -> Net-(SW54B-K)
- SW54 pad 4: unconnected-(SW54B-A-Pad4) -> HI5
- SW55 pad 3: unconnected-(SW55B-K-Pad3) -> Net-(SW55B-K)
- SW55 pad 4: unconnected-(SW55B-A-Pad4) -> HI3
- SW56 pad 3: unconnected-(SW56B-K-Pad3) -> Net-(SW56B-K)
- SW56 pad 4: unconnected-(SW56B-A-Pad4) -> HI1
- SW57 pad 3: unconnected-(SW57B-K-Pad3) -> Net-(SW57B-K)
- SW57 pad 4: unconnected-(SW57B-A-Pad4) -> HI2
- SW58 pad 3: unconnected-(SW58B-K-Pad3) -> Net-(SW58B-K)
- SW58 pad 4: unconnected-(SW58B-A-Pad4) -> HI0
- SW59 pad 3: unconnected-(SW59B-K-Pad3) -> Net-(SW59B-K)
- SW59 pad 4: unconnected-(SW59B-A-Pad4) -> HI2
- SW6 pad 3: unconnected-(SW6B-K-Pad3) -> Net-(SW6B-K)
- SW6 pad 4: unconnected-(SW6B-A-Pad4) -> HI5
- SW60 pad 3: unconnected-(SW60B-K-Pad3) -> Net-(SW60B-K)
- SW60 pad 4: unconnected-(SW60B-A-Pad4) -> HI0
- SW61 pad 3: unconnected-(SW61B-K-Pad3) -> Net-(SW61B-K)
- SW61 pad 4: unconnected-(SW61B-A-Pad4) -> HI6
- SW62 pad 3: unconnected-(SW62B-K-Pad3) -> Net-(SW62B-K)
- SW62 pad 4: unconnected-(SW62B-A-Pad4) -> HI4
- SW63 pad 3: unconnected-(SW63B-K-Pad3) -> Net-(SW63B-K)
- SW63 pad 4: unconnected-(SW63B-A-Pad4) -> HI2
- SW64 pad 3: unconnected-(SW64B-K-Pad3) -> Net-(SW64B-K)
- SW64 pad 4: unconnected-(SW64B-A-Pad4) -> HI0
- SW65 pad 3: unconnected-(SW65B-K-Pad3) -> Net-(SW65B-K)
- SW65 pad 4: unconnected-(SW65B-A-Pad4) -> HI3
- SW66 pad 3: unconnected-(SW66B-K-Pad3) -> Net-(SW66B-K)
- SW66 pad 4: unconnected-(SW66B-A-Pad4) -> HI1
- SW67 pad 3: unconnected-(SW67B-K-Pad3) -> Net-(R99-Pad1)
- SW67 pad 4: unconnected-(SW67B-A-Pad4) -> HI4
- SW68 pad 3: unconnected-(SW68B-K-Pad3) -> Net-(SW68B-K)
- SW68 pad 4: unconnected-(SW68B-A-Pad4) -> HI1
- SW69 pad 3: unconnected-(SW69B-K-Pad3) -> Net-(SW69B-K)
- SW69 pad 4: unconnected-(SW69B-A-Pad4) -> HI7
- SW7 pad 3: unconnected-(SW7B-K-Pad3) -> Net-(SW7B-K)
- SW7 pad 4: unconnected-(SW7B-A-Pad4) -> HI3
- SW70 pad 3: unconnected-(SW70B-K-Pad3) -> Net-(SW70B-K)
- SW70 pad 4: unconnected-(SW70B-A-Pad4) -> HI5
- SW71 pad 3: unconnected-(SW71B-K-Pad3) -> Net-(SW71B-K)
- SW71 pad 4: unconnected-(SW71B-A-Pad4) -> HI3
- SW72 pad 3: unconnected-(SW72B-K-Pad3) -> Net-(SW72B-K)
- SW72 pad 4: unconnected-(SW72B-A-Pad4) -> HI1
- SW73 pad 3: unconnected-(SW73B-K-Pad3) -> Net-(SW73B-K)
- SW73 pad 4: unconnected-(SW73B-A-Pad4) -> HI2
- SW74 pad 3: unconnected-(SW74B-K-Pad3) -> Net-(SW74B-K)
- SW74 pad 4: unconnected-(SW74B-A-Pad4) -> HI0
- SW75 pad 3: unconnected-(SW75B-K-Pad3) -> Net-(SW75B-K)
- SW75 pad 4: unconnected-(SW75B-A-Pad4) -> HI2
- SW76 pad 3: unconnected-(SW76B-K-Pad3) -> Net-(SW76B-K)
- SW76 pad 4: unconnected-(SW76B-A-Pad4) -> HI0
- SW77 pad 3: unconnected-(SW77B-K-Pad3) -> Net-(SW77B-K)
- SW77 pad 4: unconnected-(SW77B-A-Pad4) -> HI6
- SW78 pad 3: unconnected-(SW78B-K-Pad3) -> Net-(SW78B-K)
- SW78 pad 4: unconnected-(SW78B-A-Pad4) -> HI4
- SW79 pad 3: unconnected-(SW79B-K-Pad3) -> Net-(SW79B-K)
- SW79 pad 4: unconnected-(SW79B-A-Pad4) -> HI2
- SW8 pad 3: unconnected-(SW8B-K-Pad3) -> Net-(SW8B-K)
- SW8 pad 4: unconnected-(SW8B-A-Pad4) -> HI4
- SW80 pad 3: unconnected-(SW80B-K-Pad3) -> Net-(SW80B-K)
- SW80 pad 4: unconnected-(SW80B-A-Pad4) -> HI0
- SW9 pad 3: unconnected-(SW9B-K-Pad3) -> Net-(SW9B-K)
- SW9 pad 4: unconnected-(SW9B-A-Pad4) -> HI2

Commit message: initial placement
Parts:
- moved C4 221.3 mm to (309.2, 106.7)
- moved C3 218.5 mm to (309.1, 97.0)
- moved C6 217.2 mm to (312.3, 53.9), turned to -90 degrees
- moved C2 212.8 mm to (308.9, 87.2)
- moved C5 209.6 mm to (293.1, 95.1), turned to -90 degrees
- moved C7 197.3 mm to (292.7, 53.8), turned to -90 degrees
- moved Q6 192.9 mm to (183.4, 69.2)
- moved R3 192.9 mm to (179.6, 70.2)
- moved R6 192.9 mm to (179.6, 68.2)
- moved Q7 178.1 mm to (192.9, 88.2)
- moved R2 178.1 mm to (189.1, 89.1)
- moved R7 178.1 mm to (189.1, 87.3)
- moved Q8 168.2 mm to (197.8, 107.2)
- moved R1 168.2 mm to (194.0, 108.2)
- moved R8 168.2 mm to (194.0, 106.2)
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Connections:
- R77 pad 2: Net-(R77-Pad2) -> LO10
- R78 pad 2: Net-(R77-Pad2) -> LO10
- R79 pad 2: Net-(R77-Pad2) -> LO10
- R80 pad 2: Net-(R77-Pad2) -> LO10
- R81 pad 2: Net-(R77-Pad2) -> LO10

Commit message: PET-N r3
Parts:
- moved R49 5.21 mm to (237.0, 108.2), turned to 180 degrees
- moved R29 5.18 mm to (237.0, 106.2), turned to 180 degrees
- moved R21 5.13 mm to (323.6, 70.2), turned to 180 degrees
- moved R30 5.13 mm to (323.6, 68.1), turned to 180 degrees
- moved R28 4.97 mm to (323.4, 125.2), turned to 180 degrees
- moved R24 4.93 mm to (323.5, 127.3), turned to 180 degrees
- moved R47 4.90 mm to (260.2, 70.1), turned to 180 degrees
- moved R46 4.89 mm to (102.1, 127.6), turned to 180 degrees
- moved R44 4.88 mm to (260.2, 68.1), turned to 180 degrees
- moved R7 4.88 mm to (193.5, 89.4), turned to 180 degrees
- moved R26 4.86 mm to (323.4, 87.2), turned to 180 degrees
- moved R3 4.81 mm to (183.9, 68.2), turned to 180 degrees
- moved R6 4.81 mm to (183.9, 70.2), turned to 180 degrees
- moved R22 4.81 mm to (323.4, 89.2), turned to 180 degrees
- moved R1 4.80 mm to (198.4, 106.2), turned to 180 degrees
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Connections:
- J1 pad 29: SCA -> SDA
- SW10 pad 4: unconnected-(SW10B-A-Pad4) -> HI0
- U1 pad 15: S1 -> S0
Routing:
- net VCC: track 0.00 -> 1062.2 mm, vias 0 -> 54
- net GND: track 0.00 -> 964.2 mm, vias 0 -> 53
- net R10: track 0.00 -> 610.9 mm, vias 0 -> 10
- net R9: track 0.00 -> 600.6 mm, vias 0 -> 4
- net HI2: track 0.00 -> 551.1 mm, vias 0 -> 8
- net HI3: track 0.00 -> 494.2 mm, vias 0 -> 7
- net HI0: track 0.00 -> 488.4 mm, vias 0 -> 6
- net R2: track 0.00 -> 485.5 mm, vias 0 -> 7
- net HI1: track 0.00 -> 475.7 mm, vias 0 -> 3
- net R8: track 0.00 -> 462.7 mm, vias 0 -> 6
- net C6: track 0.00 -> 457.8 mm, vias 0 -> 4
- net R4: track 0.00 -> 455.1 mm, vias 0 -> 4
- net HI4: track 0.00 -> 449.4 mm, vias 0 -> 2
- net R7: track 0.00 -> 444.1 mm, vias 0 -> 4
- net R5: track 0.00 -> 420.0 mm, vias 0 -> 4
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- added copper zone on B.Cu, net GND
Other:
- board text added: "{dblquote}N-V3{dblquote} (C) A. Fachat, 2025-08-12"
- board text removed: "{dblquote}N-V2.1{dblquote} (C) A. Fachat, 2025-05-31"
